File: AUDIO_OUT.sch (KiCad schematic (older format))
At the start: 22 parts, among them J1 MIC_PTT, J3 Audio-Jack-3_2Switches, U16 WM8731_alt

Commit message: first module
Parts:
- removed R19: 100, UI:R_1206_0603, symbol R_Small
- removed R75, R76: 4.7k, UI:R_1206_0603, symbol R_Small
- added R? (x2): 4.7k, UI:R_1206_0603, symbol R_Small
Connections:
- net +3V3: now also R?.1, R?.1
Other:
- moved on the sheet: C49, C50, C7, D1, J1, R20, R4

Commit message: add I2S_CLKIN_MCU
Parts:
- added C5, C6: 22pF, UI:C_1206_0603, symbol C_Small
- added J5: USB_B_Mini, Connectors:USB_Mini-B, symbol USB_B_Mini
- added R?: 56, UI:R_1206_0603, symbol R_Small
- added RN6: 47, Resistors_SMD:R_Array_Convex_4x0603, symbol R_Pack04
- added Y3: 12Mhz, symbol Crystal
- gave numbers to parts that had none: 2
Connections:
- net GND: now also C5.1, C6.2, J5.5 (GND), J5.6 (Shield)
- net I2C_SCL: now also R6.2, RN6.1 (R1.1)
- net I2C_SDA: now also R5.2, RN6.2 (R2.1)
- net CLKOUT_WM8731: now reaches U16.2 (CLKOUT)
- net CLKOUT_WM8731: now also R?.1
- net at U16.25 (XTI/MCLK): now also C6.1, Y3.2
- net at U16.26 (XTO): now also C5.2, Y3.1
- new net: J5.2 (D-), RN6.3 (R3.1)
- new net: J5.3 (D+), RN6.4 (R4.1)
- new net I2C_SCL_MCU: RN6.8 (R1.2)
- new net I2C_SDA_MCU: RN6.7 (R2.2)
- new net I2S_CLKIN_MCU: R?.2
- new net USB_DM: RN6.6 (R3.2)
- new net USB_DP: RN6.5 (R4.2)
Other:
- moved on the sheet: R5, R6

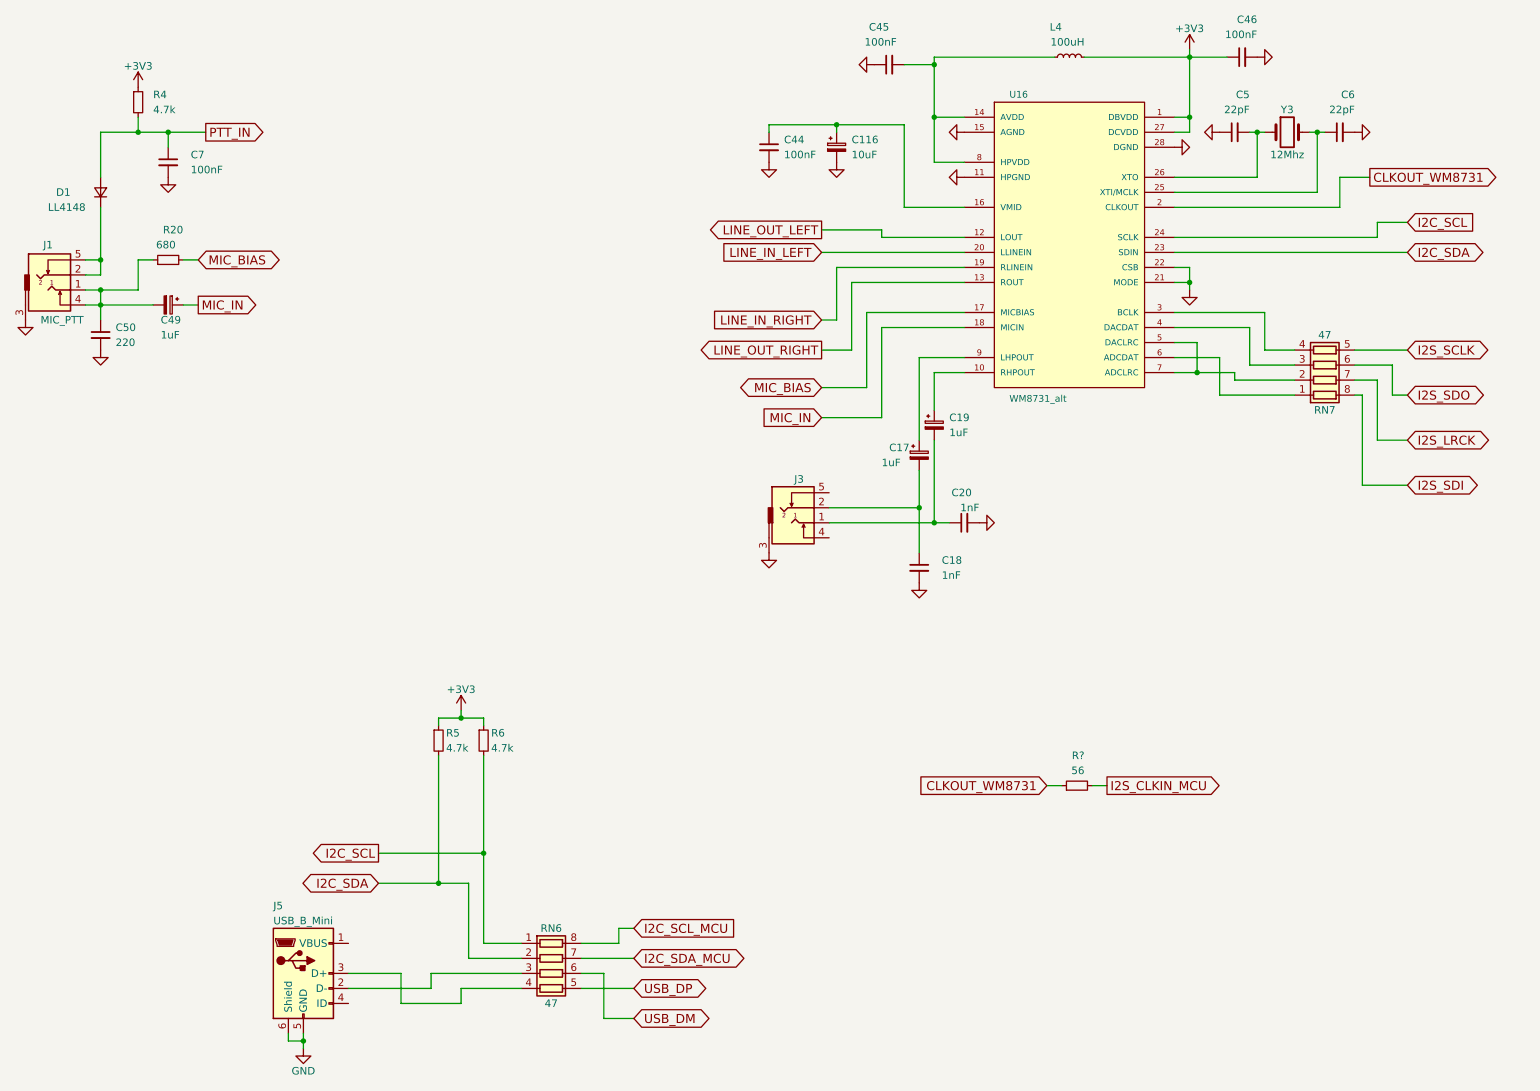
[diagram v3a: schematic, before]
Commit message: PCB almost ready, needs some GND vias
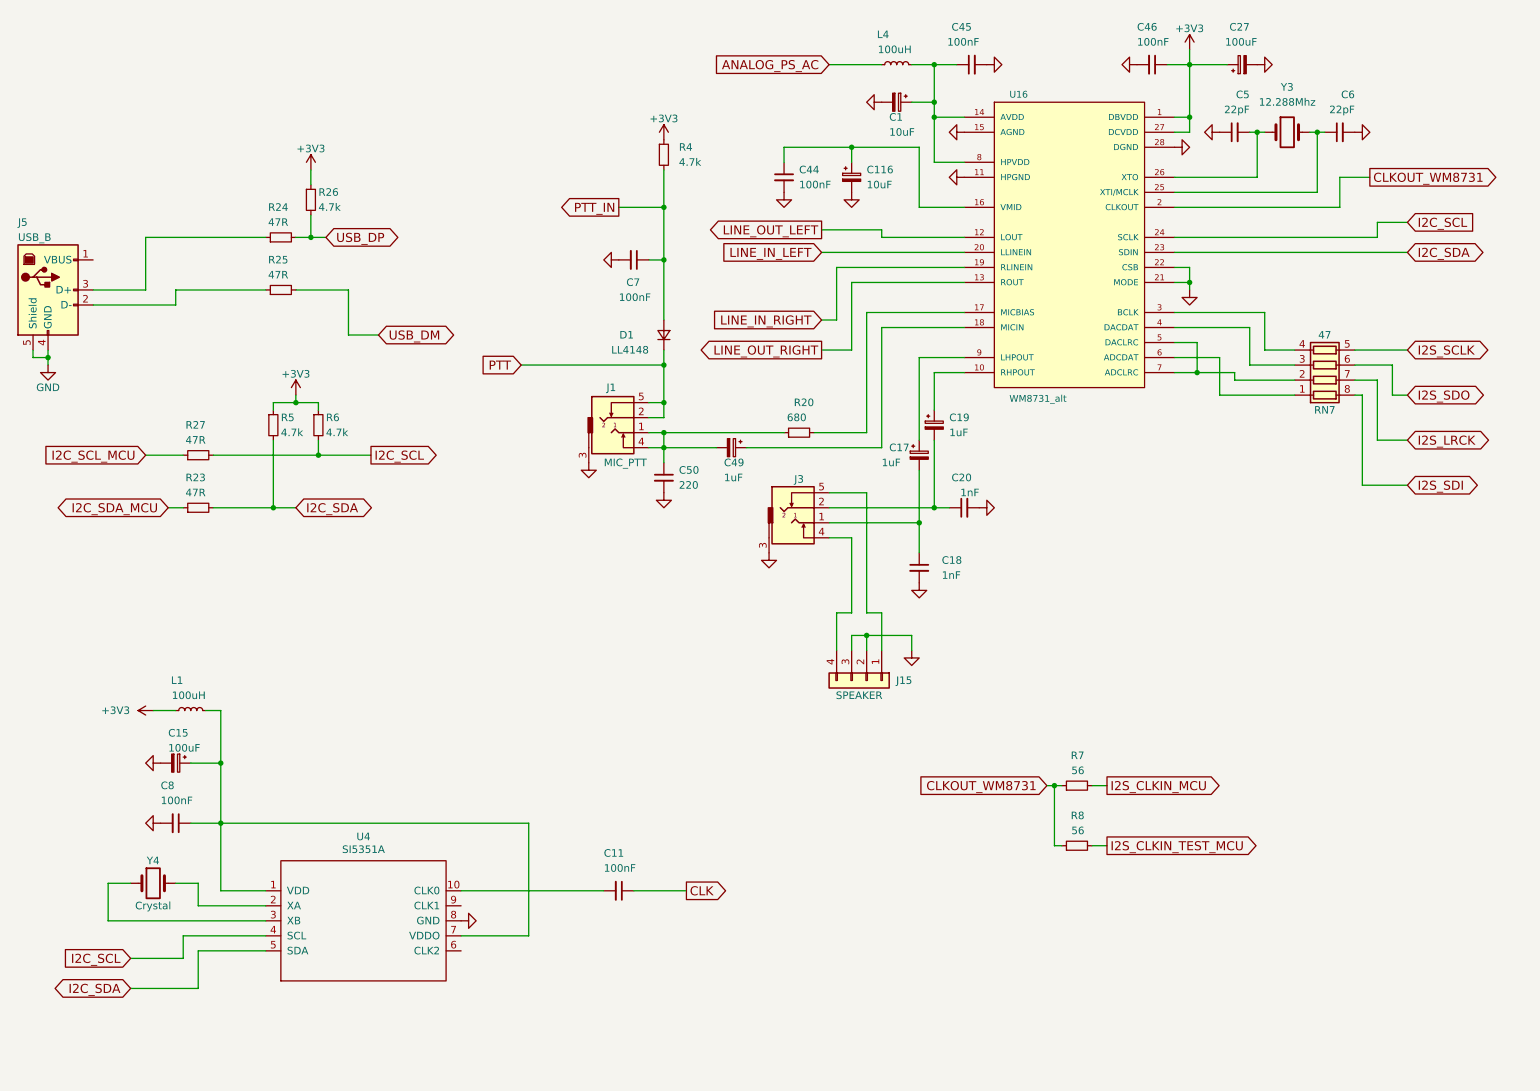
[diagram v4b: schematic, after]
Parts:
- removed J5: USB_B_Mini, Connectors:USB_Mini-B, symbol USB_B_Mini
- removed RN6: 47, Resistors_SMD:R_Array_Convex_4x0603, symbol R_Pack04
- added C1: 10uF, Capacitors_THT:CP_Radial_D5.0mm_P2.00mm, symbol CP_Small
- added C11, C8: 100nF, UI:C_1206_0603, symbol C_Small
- added C15, C27: 100uF, Capacitors_THT:CP_Radial_D6.3mm_P2.50mm, symbol CP_Small
- added J15: SPEAKER, Pin_Headers:Pin_Header_Straight_1x04_Pitch2.54mm, symbol Conn_01x04
- added J5: USB_B, Connectors:USB_B, symbol USB_B
- added L1: 100uH, Choke_Axial_ThroughHole:Choke_Horizontal_RM10mm, symbol L_Small
- added R23, R24, R25, R27: 47R, Resistors_THT:R_Axial_DIN0204_L3.6mm_D1.6mm_P7.62mm_Horizontal, symbol R_Small
- added R26: 4.7k, Resistors_THT:R_Axial_DIN0204_L3.6mm_D1.6mm_P7.62mm_Horizontal, symbol R_Small
- added R8: 56, Resistors_THT:R_Axial_DIN0204_L3.6mm_D1.6mm_P7.62mm_Horizontal, symbol R_Small
- added U4: SI5351A, Housings_SSOP:MSOP-10_3x3mm_Pitch0.5mm, symbol SI5351A
- added Y4: Crystal, Crystals:Crystal_HC49-U_Vertical, symbol Crystal
- C116: footprint Capacitors_ThroughHole:CP_Radial_D5.0mm_P2.00mm -> Capacitors_THT:CP_Radial_D5.0mm_P2.00mm
- D1: footprint Diodes_SMD:D_MiniMELF_Handsoldering -> Diodes_THT:D_DO-35_SOD27_P10.16mm_Horizontal
- R4, R5, R6: footprint UI:R_1206_0603 -> Resistors_THT:R_Axial_DIN0204_L3.6mm_D1.6mm_P7.62mm_Horizontal
- R7: renamed from R?; footprint UI:R_1206_0603 -> Resistors_THT:R_Axial_DIN0204_L3.6mm_D1.6mm_P7.62mm_Horizontal
- Y3: value 12Mhz -> 12.288Mhz; footprint (none) -> Crystals:Crystal_HC49-U_Vertical
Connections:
- net +3V3: now also C27.1, L1.1, R26.1; no longer L4.2
- net CLKOUT_WM8731: now also R8.1
- net GND: now also C45.2, C1.2, C15.2, C27.2, C8.2, J15.2 (Pin_2), J15.3 (Pin_3), J5.4 (GND), J5.5 (Shield), U4.8 (GND); no longer C45.1
- net I2C_SCL: now also R27.2, U4.4 (SCL)
- net I2C_SCL_MCU: now also R27.1
- net I2C_SDA: now also R23.2, U4.5 (SDA)
- net I2C_SDA_MCU: now also R23.1
- net USB_DM: now also R25.2
- net USB_DP: now also R24.2, R26.2
- net at U16.14 (AVDD), U16.8 (HPVDD): now also C45.1, L4.2, C1.1; no longer C45.2, L4.1
- net at C19.2, C20.1: now also J3.2; no longer J3.1
- net at C17.2, C18.1: now also J3.1; no longer J3.2
- net at J3.4: now also J15.4 (Pin_4)
- net at J3.5: now also J15.1 (Pin_1)
- net PTT: now reaches D1.1 (K), J1.2, J1.5
- net MIC_BIAS: no longer names the net of R20.2, U16.17 (MICBIAS)
- net MIC_IN: no longer names the net of C49.1, U16.18 (MICIN)
- new net: C15.1, C8.1, L1.2, U4.1 (VDD), U4.7 (VDDO)
- new net: C11.2, U4.10 (CLK0)
- new net: U4.2 (XA), Y4.2
- new net: U4.3 (XB), Y4.1
- new net: J5.2 (D-), R25.1
- new net: J5.3 (D+), R24.1
- new net ANALOG_PS_AC: L4.1
- new net CLK: C11.1
- new net I2S_CLKIN_TEST_MCU: R8.2
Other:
- moved on the sheet: C116, C20, C44, C45, C46, C49, C50, C7, D1, J1, L4, R20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

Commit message: PCB for 98.304Mhz generator
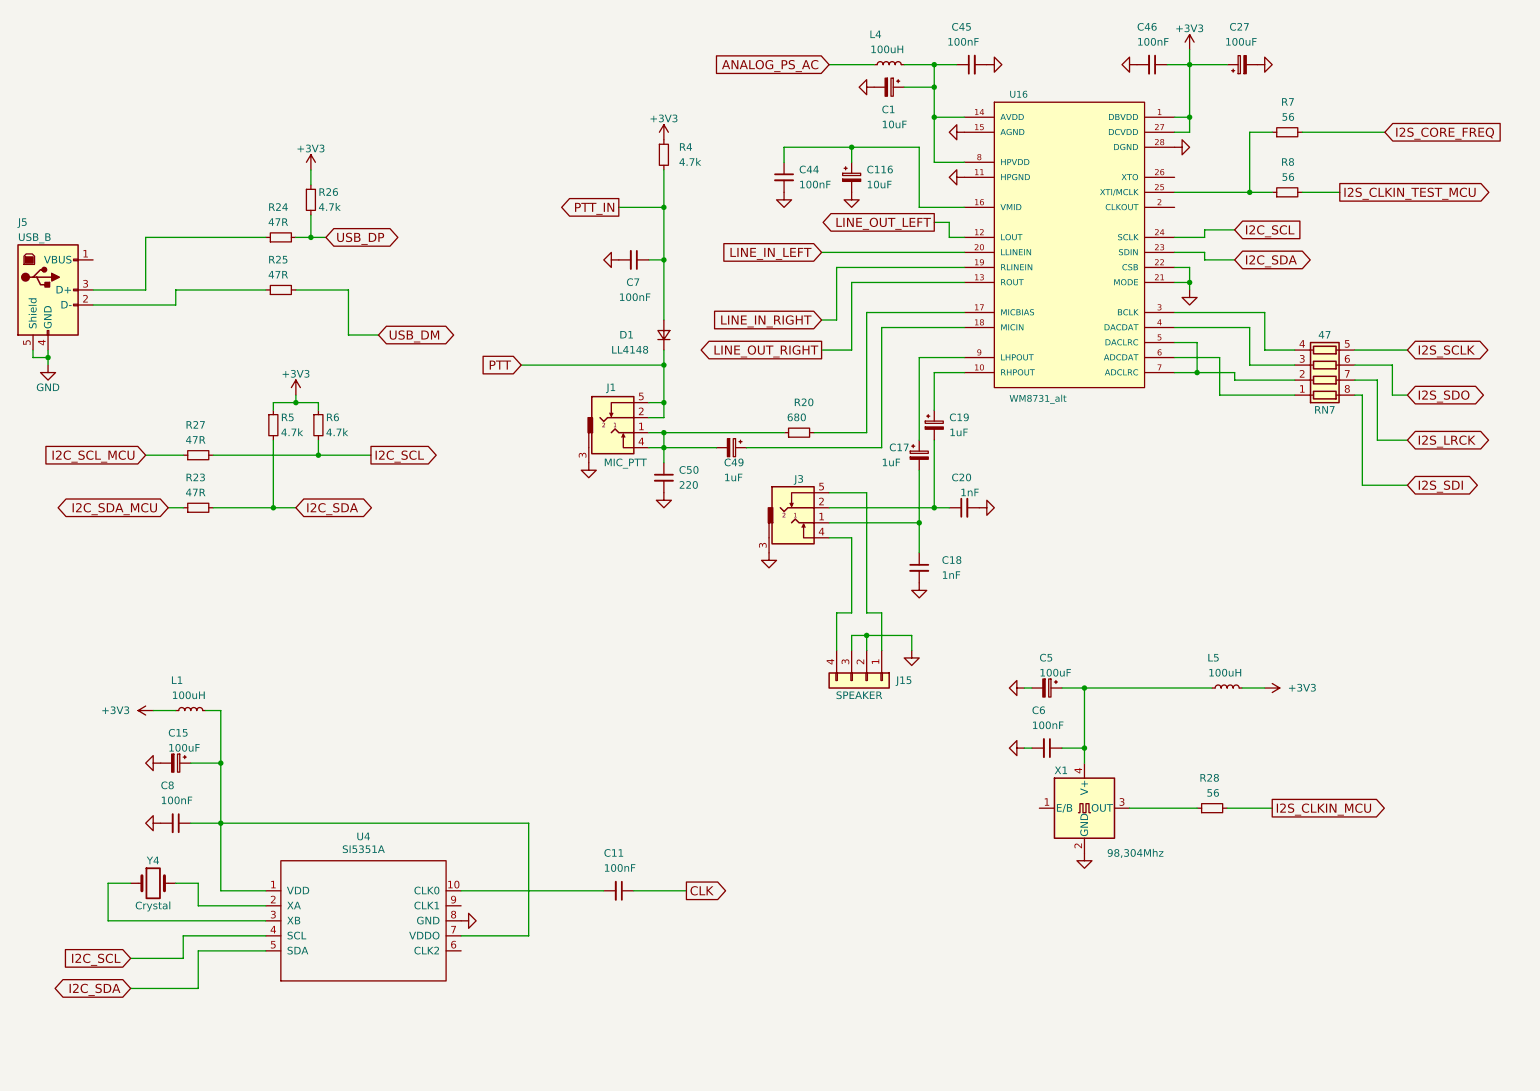
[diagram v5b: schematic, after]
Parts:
- removed C5: 22pF, UI:C_1206_0603, symbol C_Small
- removed Y3: 12.288Mhz, Crystals:Crystal_HC49-U_Vertical, symbol Crystal
- added C5: 100uF, Capacitors_THT:CP_Radial_D6.3mm_P2.50mm, symbol CP_Small
- added L5: 100uH, Choke_Axial_ThroughHole:Choke_Horizontal_RM10mm, symbol L_Small
- added R28: 56, Resistors_THT:R_Axial_DIN0204_L3.6mm_D1.6mm_P7.62mm_Horizontal, symbol R_Small
- added X1: 98,304Mhz, Oscillators:Oscillator_SMD_IQD_IQXO70-4pin_7.5x5.0mm, symbol IQXO-70
- C6: value 22pF -> 100nF
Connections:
- net +3V3: now also L5.2
- net GND: now also C5.2, X1.2 (GND)
- net I2S_CLKIN_MCU: now also R28.2; no longer R7.2
- net at U16.25 (XTI/MCLK): now also R7.1, R8.1; no longer C6.1
- removed net CLKOUT_WM8731: R7.1, R8.1, U16.2 (CLKOUT)
- new net: R28.1, X1.3 (OUT)
- new net: C5.1, C6.1, L5.1, X1.4 (V+)
- new net I2S_CORE_FREQ: R7.2
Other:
- moved on the sheet: C1, L4, R7, R8
